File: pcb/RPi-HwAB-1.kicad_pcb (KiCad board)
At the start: 6 copper layers, 65 x 56 mm, 131 parts, among them J1 GPIO, J2 Hirose_FH12-16S, J3 TC2030, U1 CAT24C256, U10 MT41K256M16TW-107:P TR, U11 INA230AIRGTR, U12 MCP9804T-E/MC, U13 INA230AIRGTR, U14 INA230AIRGTR, U2 TPSM82903, U3 TLV74312PDBVR, U4 TPSM82903, U5 AP3441SHE-7B, U6 AP3441SHE-7B, U7 XC7A100T-FGG484, U9 MX25L12835F, Y1 SiT9365AI-2B2-33E200.000000

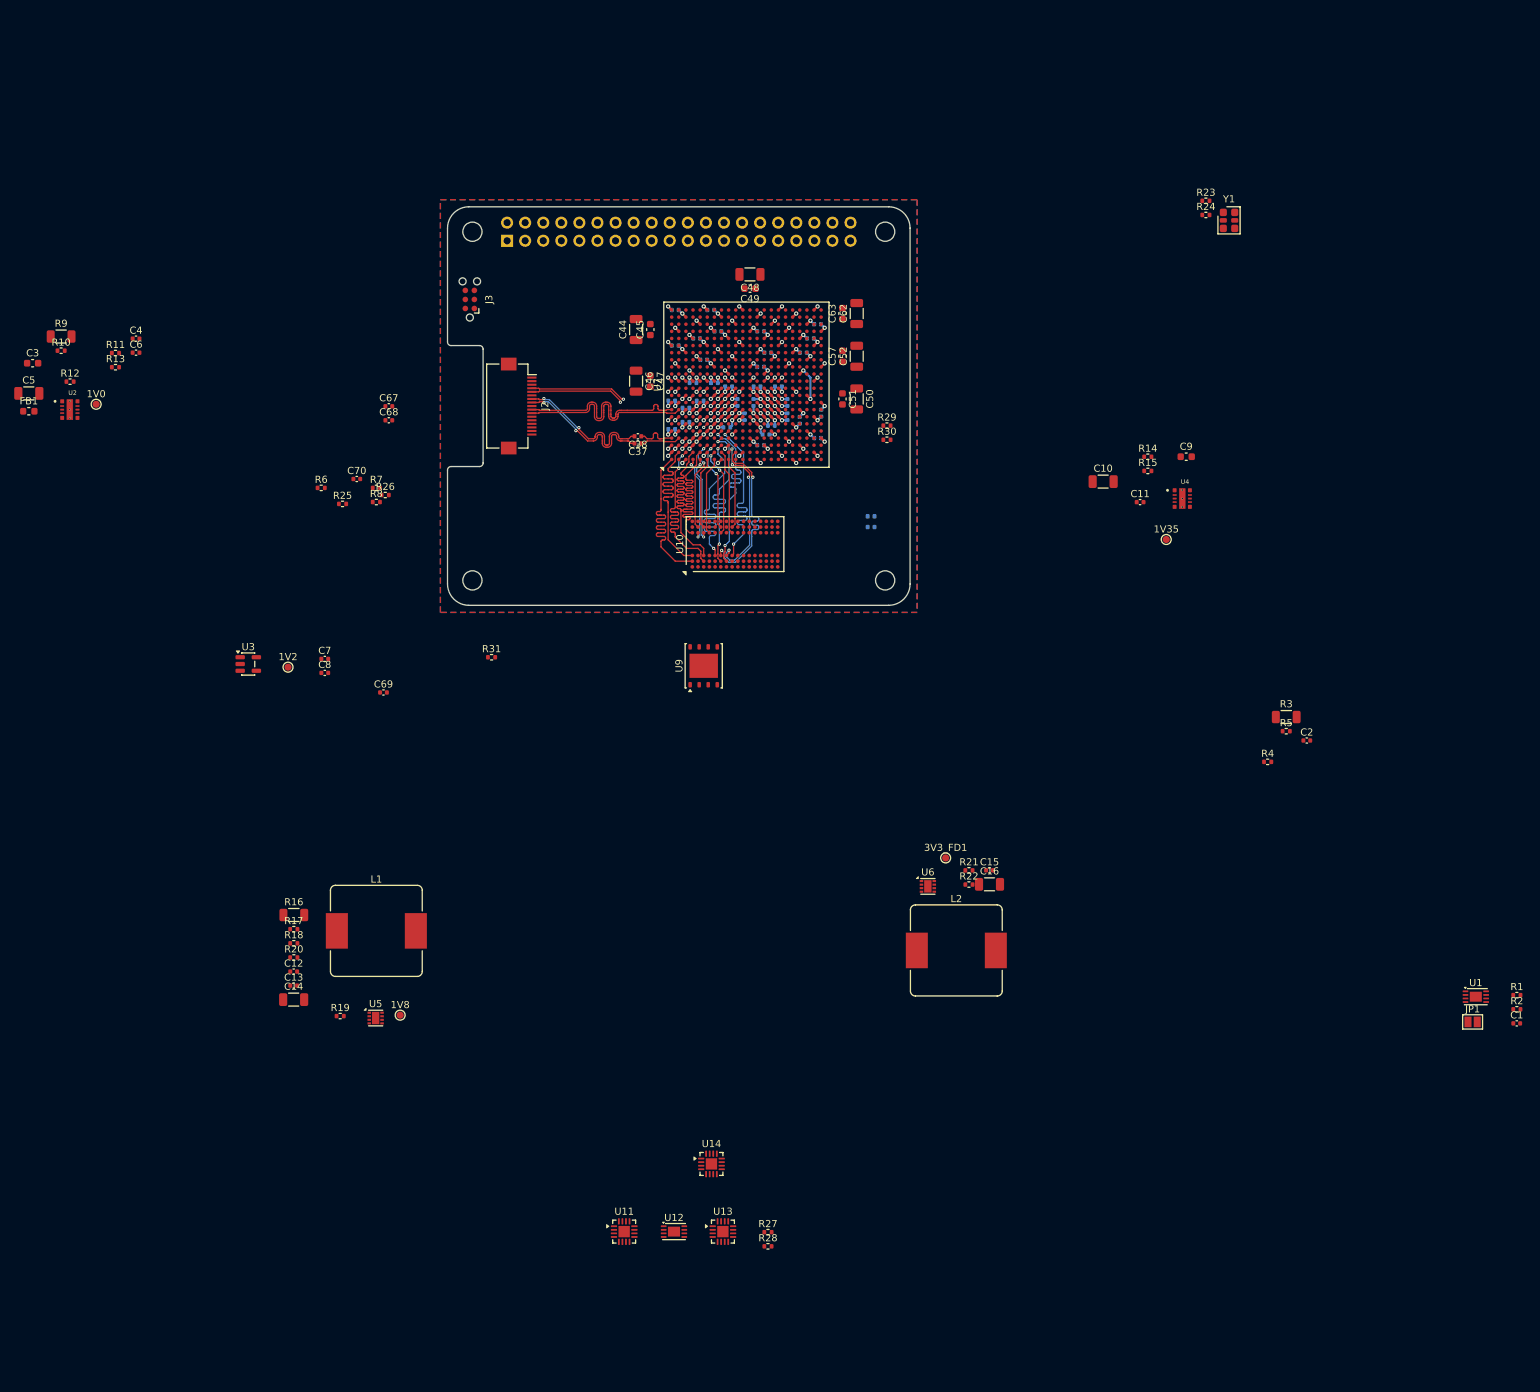
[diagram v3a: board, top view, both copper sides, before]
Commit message: restructured power, power plane layout
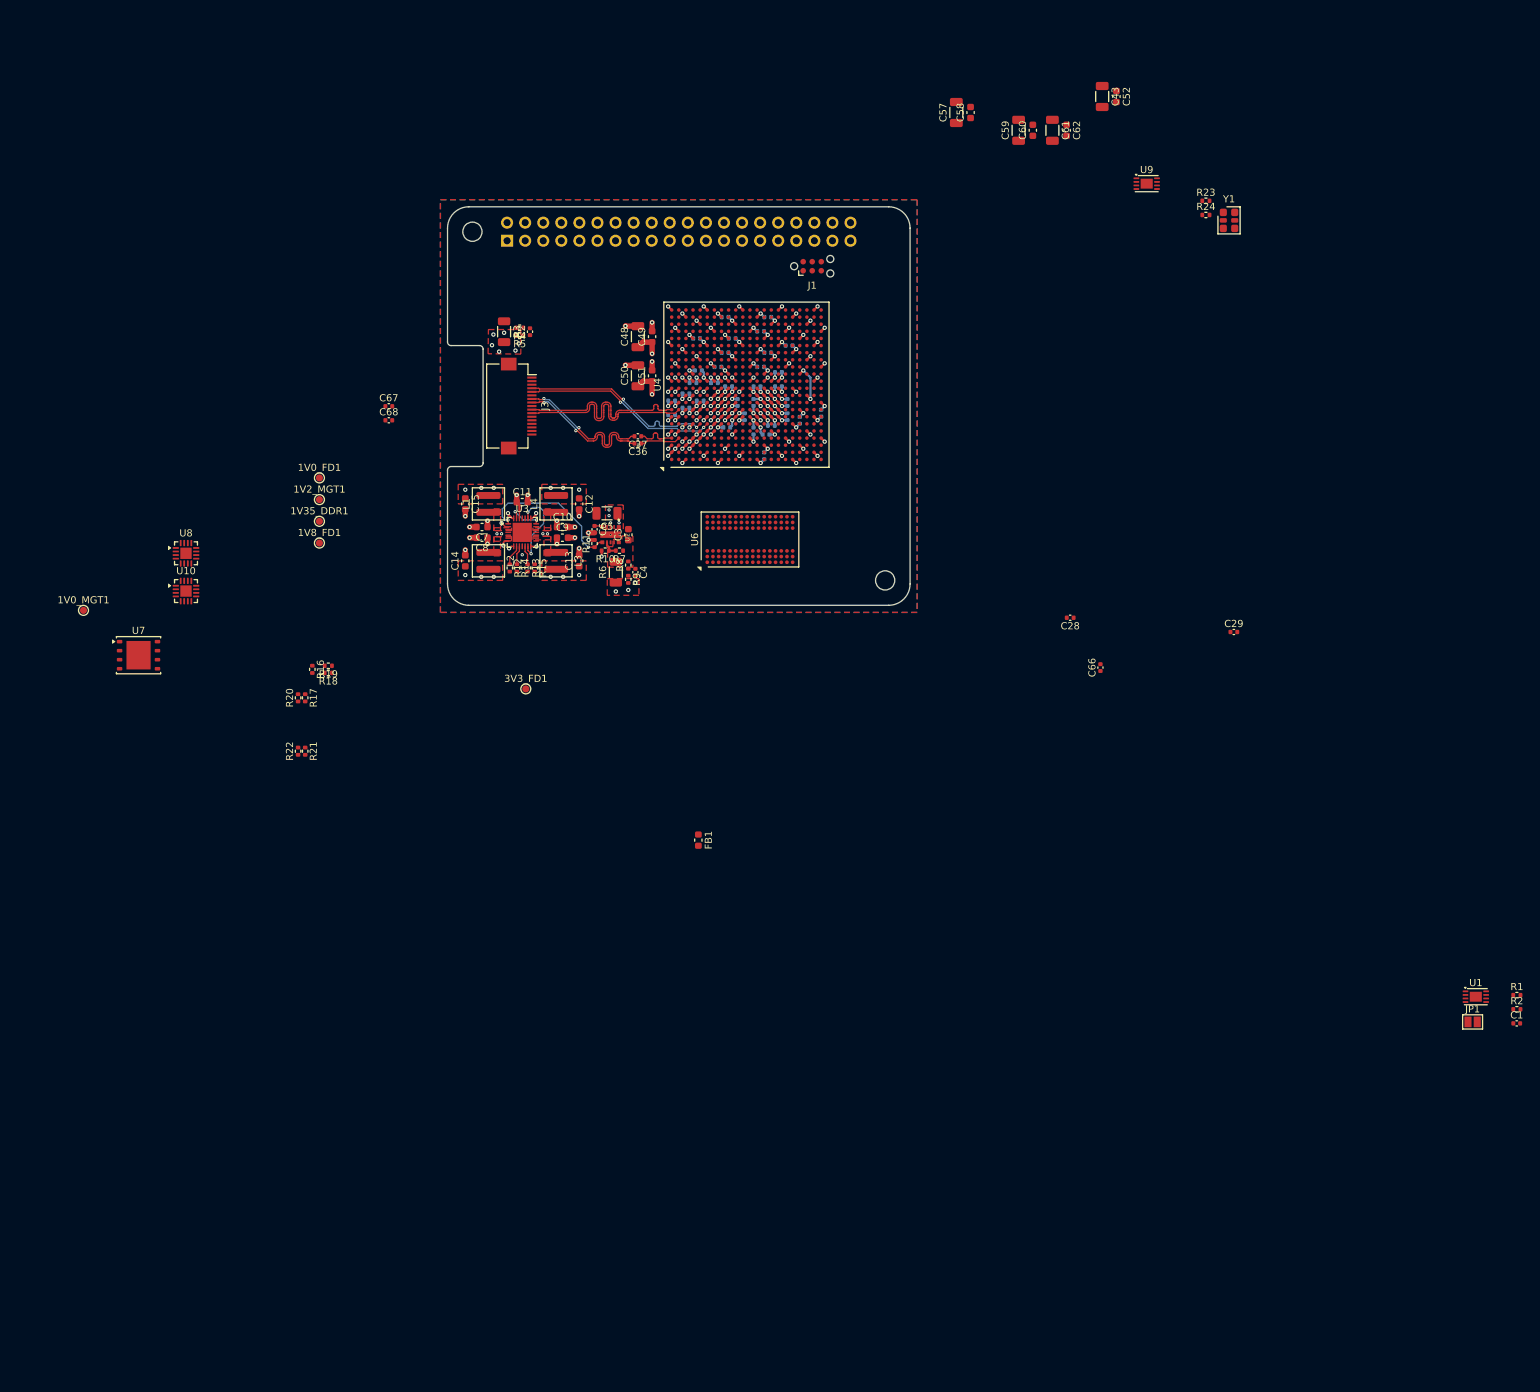
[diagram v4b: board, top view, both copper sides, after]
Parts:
- removed 1V0, 1V2, 1V35, 1V8: TestPoint, TestPoint:TestPoint_Pad_D1.0mm
- removed C69, C70: 0.1uF, Capacitor_SMD:C_0402_1005Metric
- removed MH2, MH3: MountingHole_2.7mm_M2.5, MountingHole:MountingHole_2.7mm_M2.5
- removed R25: 1K, Resistor_SMD:R_0402_1005Metric
- removed R26: 240 1%, Resistor_SMD:R_0402_1005Metric
- removed R27, R28: 4.7K, Resistor_SMD:R_0402_1005Metric
- removed R29: 2.2K, Resistor_SMD:R_0402_1005Metric
- removed R30: 100K, Resistor_SMD:R_0402_1005Metric
- removed R31: 100 1%, Resistor_SMD:R_0402_1005Metric
- removed U11, U13, U14: INA230AIRGTR, Package_DFN_QFN:VQFN-16-1EP_3x3mm_P0.5mm_EP1.6x1.6mm
- removed U12: MCP9804T-E/MC, Package_DFN_QFN:DFN-8-1EP_3x2mm_P0.5mm_EP1.7x1.4mm
- removed U5: AP3441SHE-7B, Package_DFN_QFN:DFN-8-1EP_2x2mm_P0.5mm_EP1.05x1.75mm
- added 1V0_FD1: TestPoint, TestPoint:TestPoint_Pad_D1.0mm, F.Cu at (82.0, 82.1)
- added 1V0_MGT1: TestPoint, TestPoint:TestPoint_Pad_D1.0mm, F.Cu at (48.8, 100.7)
- added 1V2_MGT1: TestPoint, TestPoint:TestPoint_Pad_D1.0mm, F.Cu at (82.0, 85.2)
- added 1V35_DDR1: TestPoint, TestPoint:TestPoint_Pad_D1.0mm, F.Cu at (82.0, 88.2)
- added 1V8_FD1: TestPoint, TestPoint:TestPoint_Pad_D1.0mm, F.Cu at (82.0, 91.2)
- added L3: 1.5uH, Inductor_SMD:L_Coilcraft_XAL4020-XXX, F.Cu at (115.2, 93.8)
- added L4: 1.5uH, Inductor_SMD:L_Coilcraft_XAL4020-XXX, F.Cu at (115.2, 85.8)
- added U8: INA230AIRGTR, Package_DFN_QFN:VQFN-16-1EP_3x3mm_P0.5mm_EP1.6x1.6mm, F.Cu at (63.2, 92.7)
- C10: value 10uF -> 2.2uF; footprint Capacitor_SMD:C_1206_3216Metric -> Capacitor_SMD:C_0603_1608Metric
- C11: value 4.7nF -> 2.2uF; footprint Capacitor_SMD:C_0402_1005Metric -> Capacitor_SMD:C_0603_1608Metric
- C12, C15: value 4.7nF -> 22uF; footprint Capacitor_SMD:C_0402_1005Metric -> Capacitor_SMD:C_0603_1608Metric
- C13: value 0.1uF -> 22uF; footprint Capacitor_SMD:C_0402_1005Metric -> Capacitor_SMD:C_0603_1608Metric
- C14: value 10uF -> 22uF; footprint Capacitor_SMD:C_1206_3216Metric -> Capacitor_SMD:C_0603_1608Metric
- C16, C44, C46: value 10uF -> 0.1uF; footprint Capacitor_SMD:C_1206_3216Metric -> Capacitor_SMD:C_0402_1005Metric; moved to B.Cu
- C28, C29, C36, C66: moved to F.Cu
- C38: moved to B.Cu
- C43, C59, C61: value 0.1uF -> 10uF; footprint Capacitor_SMD:C_0402_1005Metric -> Capacitor_SMD:C_1206_3216Metric; moved to F.Cu
- C45, C47, C63: value 4.7uF -> 0.1uF; footprint Capacitor_SMD:C_0603_1608Metric -> Capacitor_SMD:C_0402_1005Metric; moved to B.Cu
- C52, C62: value 10uF -> 4.7uF; footprint Capacitor_SMD:C_1206_3216Metric -> Capacitor_SMD:C_0603_1608Metric
- C57: value 4.7uF -> 10uF; footprint Capacitor_SMD:C_0603_1608Metric -> Capacitor_SMD:C_1206_3216Metric
- C58, C60: value 0.1uF -> 4.7uF; footprint Capacitor_SMD:C_0402_1005Metric -> Capacitor_SMD:C_0603_1608Metric; moved to F.Cu
- C7, C8: value 1uF -> 2.2uF; footprint Capacitor_SMD:C_0402_1005Metric -> Capacitor_SMD:C_0603_1608Metric
- C9: value 22uF -> 2.2uF
- L1, L2: value 2.2uH -> 1.5uH; footprint Inductor_SMD:L_Bourns_SRP1245A -> Inductor_SMD:L_Coilcraft_XAL4020-XXX
- R10: value 10K 1% -> 15K 1%
- R11, R12: value 10 -> 20K
- R13, R14: value 15K 1% -> 20K
- R15: value 12K 1% -> 20K
- R16: value 0.005 -> 100 1%; footprint Resistor_SMD:R_1206_3216Metric -> Resistor_SMD:R_0402_1005Metric
- R17: value 30K 1% -> 4.7K
- R18: value 10 -> 4.7K
- R19: value 10 -> 1K
- R20: value 15K 1% -> 240 1%
- R21: value 113K 1% -> 4.7K
- R22: value 24.9K 1% -> 4.7K
- R23: value 4.7K -> 2.2K
- R24: value 4.7K -> 100K
- R6: value 100K -> 0.005; footprint Resistor_SMD:R_0402_1005Metric -> Resistor_SMD:R_1206_3216Metric
- R7: value 100K -> 10K 1%
- R8: value 100K -> 10
- R9: value 0.005 -> 10; footprint Resistor_SMD:R_1206_3216Metric -> Resistor_SMD:R_0402_1005Metric
- U10: value MT41K256M16TW-107:P TR -> INA230AIRGTR; footprint Package_BGA:Micron_FBGA-96_7.5x13.5mm_Layout9x16_P0.8mm -> Package_DFN_QFN:VQFN-16-1EP_3x3mm_P0.5mm_EP1.6x1.6mm
- U3: value TLV74312PDBVR -> MAX20029; footprint Package_TO_SOT_SMD:SOT-23-5 -> Package_DFN_QFN:WQFN-28-1EP_4x4mm_P0.4mm_EP2.7x2.7mm
- U4: value TPSM82903 -> XC7A100T-FGG484; footprint library:TPSM82903SISR -> library:Xilinx_FGG484
- U6: value AP3441SHE-7B -> MT41K256M16TW-107:P TR; footprint Package_DFN_QFN:DFN-8-1EP_2x2mm_P0.5mm_EP1.05x1.75mm -> Package_BGA:Micron_FBGA-96_7.5x13.5mm_Layout9x16_P0.8mm
- U7: value XC7A100T-FGG484 -> MX25L12835F; footprint library:Xilinx_FGG484 -> Package_SON:WSON-8-1EP_6x5mm_P1.27mm_EP3.4x4mm
- U9: value MX25L12835F -> MCP9804T-E/MC; footprint Package_SON:WSON-8-1EP_6x5mm_P1.27mm_EP3.4x4mm -> Package_DFN_QFN:DFN-8-1EP_3x2mm_P0.5mm_EP1.7x1.4mm
- moved C2 123.4 mm to (111.6, 61.5), turned to 90 degrees
- moved R3 122.5 mm to (108.0, 61.5), turned to -90 degrees
- moved R4 121.5 mm to (110.1, 61.0), turned to 180 degrees
- moved R5 121.2 mm to (110.1, 62.1), turned to 180 degrees
- moved FB1 111.7 mm to (135.2, 133.0), turned to -90 degrees
- moved R22 96.1 mm to (79.0, 120.5), turned to 90 degrees
- moved R21 94.8 mm to (80.0, 120.5), turned to -90 degrees
- moved U7 93.5 mm to (56.6, 107.0), turned to 0 degrees
- moved U9 92.0 mm to (198.2, 40.8), turned to 0 degrees
- moved R14 90.0 mm to (109.8, 94.8), turned to -90 degrees
- moved C15 89.9 mm to (102.5, 85.8), turned to -90 degrees
- moved C9 88.4 mm to (116.2, 90.5)
- moved R15 87.2 mm to (112.2, 94.8), turned to -90 degrees
- moved C3 87.1 mm to (125.4, 90.1), turned to 90 degrees
- moved C11 86.8 mm to (110.5, 85.5)
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- renumbered J3 to J1, J1 to J2, J2 to J3
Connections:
- C11 pad 1: Net-(U4-SS/TR) -> /Main Power/5V0_N
- C12 pad 1: /Main Power/1V8/1V8_P -> /Main Power/1V2_MGT
- C12 pad 2: /Main Power/1V8/1V8_FB -> GND
- C13 pad 1: /Main Power/1V8_SENS_N -> /Main Power/3V3_FD
- C13 pad 2: /Main Power/1V8_SENS_P -> GND
- C14 pad 1: /Main Power/5V0_N -> /Main Power/1V35_DDR
- C15 pad 1: /Main Power/3V3_FD -> /Main Power/1V8_FD
- C15 pad 2: /Main Power/3V3/3V3_FB -> GND
- C16 pad 1: /Main Power/5V0_N -> GND
- C16 pad 2: GND -> /Main Power/3V3_FD
- C28 pad 1: GND -> /FPGA/FPGA 34, 35/DDR_SYSCLK_N
- C28 pad 2: /Main Power/3V3_FD -> Net-(Y1-OUT-)
- C29 pad 1: /FPGA/FPGA 3/DDR_SYSCLK_N -> /FPGA/FPGA 34, 35/DDR_SYSCLK_P
- C29 pad 2: Net-(Y1-OUT-) -> Net-(Y1-OUT+)
- C30 pad 1: /FPGA/FPGA 3/DDR_SYSCLK_P -> GND
- C30 pad 2: Net-(Y1-OUT+) -> /Main Power/1V35_DDR
- C36 pad 1: GND -> /FPGA/FPGA 216/F2P_P
- C36 pad 2: /Main Power/1V35_DDR -> /Connectors/PCIE.F2P_N
- C37 pad 1: /FPGA/FPGA 4/F2P_P -> /FPGA/FPGA 216/F2P_N
- C37 pad 2: /Connectors/PCIE.F2P_N -> /Connectors/PCIE.F2P_P
- C38 pad 1: /FPGA/FPGA 4/F2P_N -> GND
- C38 pad 2: /Connectors/PCIE.F2P_P -> /Main Power/1V0_MGT
- C40 pad 2: /Main Power/1V0_MGT -> /Main Power/1V2_MGT
- C43 pad 1: GND -> /Main Power/1V0_FD
- C43 pad 2: /Main Power/1V2_MGT -> GND
- C44 pad 1: /Main Power/1V0_MGT -> GND
- C44 pad 2: GND -> /Main Power/1V0_FD
- C45 pad 1: /Main Power/1V0_MGT -> GND
- C45 pad 2: GND -> /Main Power/1V0_FD
- C46 pad 1: /Main Power/1V2_MGT -> GND
- C46 pad 2: GND -> /Main Power/1V0_FD
- C47 pad 1: /Main Power/1V2_MGT -> GND
- C47 pad 2: GND -> /Main Power/1V0_FD
- C48 pad 1: /Main Power/3V3_FD -> /Main Power/1V0_MGT
- C49 pad 1: /Main Power/3V3_FD -> /Main Power/1V0_MGT
- C50 pad 1: /Main Power/1V35_DDR -> /Main Power/1V2_MGT
- C51 pad 1: /Main Power/1V35_DDR -> /Main Power/1V2_MGT
- C57 pad 1: /Main Power/1V0_FD -> /Main Power/3V3_FD
- C58 pad 1: GND -> /Main Power/3V3_FD
- C58 pad 2: /Main Power/1V0_FD -> GND
- C59 pad 1: GND -> /Main Power/1V35_DDR
- C59 pad 2: /Main Power/1V0_FD -> GND
- C60 pad 1: GND -> /Main Power/1V35_DDR
- C60 pad 2: /Main Power/1V0_FD -> GND
- C61 pad 1: GND -> /Main Power/1V8_FD
- C61 pad 2: /Main Power/1V0_FD -> GND
- C63 pad 1: /Main Power/1V8_FD -> GND
- C63 pad 2: GND -> /Main Power/1V8_FD
- C66 pad 1: GND -> /Connectors/3V3_RPi
- C66 pad 2: /Main Power/1V8_FD -> GND
- C7 pad 1: /Main Power/1V8_FD -> /Main Power/5V0_N
- C8 pad 1: /Main Power/1V2_MGT -> /Main Power/5V0_N
- C9 pad 1: /Main Power/1V35_DDR -> /Main Power/5V0_N
- J2 pad 18: /Main Power/3V3/3V3_PG -> /Connectors/FPGA_PG
- L1 pad 1: /Main Power/1V8/1V8_LX -> /Main Power/Quad Buck/LX1
- L1 pad 2: /Main Power/1V8/1V8_P -> /Main Power/1V8_FD
- L2 pad 1: /Main Power/3V3/3V3_LX -> /Main Power/Quad Buck/LX2
- L2 pad 2: /Main Power/3V3_FD -> /Main Power/1V35_DDR
- R10 pad 1: /Main Power/1V0/1V0_P -> /Main Power/1V0/1V0_FB
- R10 pad 2: /Main Power/1V0/1V0_FB -> GND
- R11 pad 1: /Main Power/1V0_SENS_N -> /Main Power/1V0/1V0_PG
- R11 pad 2: /Main Power/1V0/1V0_P -> /Main Power/5V0_N
- R12 pad 1: /Main Power/1V0_SENS_P -> /Main Power/Quad Buck/1V2_PG
- R12 pad 2: /Main Power/1V0_FD -> /Main Power/5V0_N
- R13 pad 1: /Main Power/1V0/1V0_FB -> /Main Power/Quad Buck/3V3_PG
- R13 pad 2: GND -> /Main Power/5V0_N
- R14 pad 1: /Main Power/1V35_DDR -> /Main Power/Quad Buck/1V35_PG
- R14 pad 2: /Main Power/1V35/1V35_FB -> /Main Power/5V0_N
- R15 pad 1: /Main Power/1V35/1V35_FB -> /Main Power/Quad Buck/1V8_PG
- R15 pad 2: GND -> /Main Power/5V0_N
- R16 pad 1: /Main Power/1V8_FD -> /FPGA/FPGA 34, 35/DDR_SYSCLK_N
- R16 pad 2: /Main Power/1V8/1V8_P -> /FPGA/FPGA 34, 35/DDR_SYSCLK_P
- R17 pad 1: /Main Power/1V8/1V8_P -> /Main Power/1V35_DDR
- R17 pad 2: /Main Power/1V8/1V8_FB -> /FPGA/FPGA 34, 35/DDR_SYSCLK_P
- R18 pad 1: /Main Power/1V8_SENS_P -> /FPGA/FPGA 34, 35/DDR_SYSCLK_P
- R18 pad 2: /Main Power/1V8/1V8_P -> GND
- R19 pad 1: /Main Power/1V8_SENS_N -> Net-(U4G-MGTRREF_216)
- R19 pad 2: /Main Power/1V8_FD -> /Main Power/1V2_MGT
- R20 pad 1: /Main Power/1V8/1V8_FB -> Net-(U6-ZQ)
- R20 pad 2: GND -> /Main Power/1V35_DDR
- R21 pad 1: /Main Power/3V3_FD -> /Connectors/3V3_RPi
- R21 pad 2: /Main Power/3V3/3V3_FB -> /Connectors/I2C1.SDA
- R22 pad 1: /Main Power/3V3/3V3_FB -> /Connectors/3V3_RPi
- R22 pad 2: GND -> /Connectors/I2C1.SCL
- R23 pad 1: /Main Power/1V35_DDR -> /Main Power/3V3_FD
- R23 pad 2: /FPGA/FPGA 3/DDR_SYSCLK_P -> /Connectors/PCIE.DET_WAKE
- R24 pad 1: /FPGA/FPGA 3/DDR_SYSCLK_P -> GND
- R24 pad 2: GND -> /Connectors/PCIE.PWR_EN
- R6 pad 1: /Main Power/5V0_N -> /Main Power/1V0_FD
- R6 pad 2: /Main Power/1V0/1V0_PG -> /Main Power/1V0/1V0_P
- R7 pad 1: /Main Power/5V0_N -> /Main Power/1V0/1V0_P
- R7 pad 2: /Main Power/1V8/1V8_PG -> /Main Power/1V0/1V0_FB
- R8 pad 1: /Main Power/5V0_N -> /Main Power/1V0_SENS_N
- R8 pad 2: /Main Power/3V3/3V3_PG -> /Main Power/1V0/1V0_P
- R9 pad 1: /Main Power/1V0_FD -> /Main Power/1V0_SENS_P
- R9 pad 2: /Main Power/1V0/1V0_P -> /Main Power/1V0_FD
- U3 pad 1: /Main Power/1V8_FD -> /Main Power/1V0/1V0_PG
- U3 pad 2: GND -> /Main Power/5V0_N
- U3 pad 3: /Main Power/1V8_FD -> /Main Power/Quad Buck/LX1
- U3 pad 4: unconnected-(U3-NC-Pad4) -> GND
- U3 pad 5: /Main Power/1V2_MGT -> GND
- U9 pad 1: /Connectors/QSPI0.CS0n -> /Connectors/I2C1.SDA
- U9 pad 2: /Connectors/QSPI0.SIO1 -> /Connectors/I2C1.SCL
- U9 pad 3: /Connectors/QSPI0.SIO2 -> unconnected-(U9-Alert-Pad3)
- U9 pad 5: /Connectors/QSPI0.SIO0 -> GND
- U9 pad 6: /Connectors/QSPI0.SCLK -> GND
- U9 pad 7: /Connectors/QSPI0.SIO3 -> GND
- U9 pad 8: /Main Power/3V3_FD -> /Connectors/3V3_RPi
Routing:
- net /FPGA/FPGA 3/DQ13: track 26.7 -> 0.00 mm
- net /FPGA/FPGA 3/DQ15: track 26.7 -> 0.00 mm
- net /FPGA/FPGA 3/DQ9: track 26.7 -> 0.00 mm
- net /FPGA/FPGA 3/DQ12: track 26.7 -> 0.00 mm
- net /FPGA/FPGA 3/DDR_LDQS_P: track 25.3 -> 0.00 mm, vias 2 -> 0
- net /FPGA/FPGA 3/DQ2: track 25.3 -> 0.00 mm, vias 2 -> 0
- net /FPGA/FPGA 3/DQ6: track 25.3 -> 0.00 mm, vias 2 -> 0
- net /FPGA/FPGA 3/DQ4: track 25.3 -> 0.00 mm, vias 2 -> 0
- net /FPGA/FPGA 3/DQ11: track 25.2 -> 0.00 mm, vias 2 -> 0
- net /FPGA/FPGA 3/DQ0: track 25.2 -> 0.00 mm, vias 2 -> 0
- net /FPGA/FPGA 3/DDR_LDQS_N: track 22.5 -> 0.00 mm, vias 4 -> 0
- net /Main Power/1V0/1V0_PG: track 0.00 -> 21.1 mm, vias 0 -> 2
- net GND: track 106.1 -> 122.0 mm, vias 90 -> 110
- net /Main Power/Quad Buck/1V2_PG: track 0.00 -> 14.4 mm, vias 0 -> 2
- net /FPGA/FPGA 3/DQ14: track 13.0 -> 0.00 mm, vias 2 -> 0
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- added copper zone on F.Cu, net /Main Power/1V0/1V0_P
- added copper zone on F.Cu, net /Main Power/1V0_FD
- added copper zone on F.Cu, net /Main Power/1V2_MGT
- added copper zone on F.Cu, net /Main Power/1V35_DDR
- added copper zone on F.Cu, net /Main Power/1V8_FD
- added copper zone on F.Cu, net /Main Power/3V3_FD
- added copper zone on F.Cu, net /Main Power/5V0_N
- added copper zone on In2.Cu, net /Main Power/5V0_N
- added copper zone on F.Cu, net /Main Power/Quad Buck/LX1
- added copper zone on F.Cu, net /Main Power/Quad Buck/LX2
- added copper zone on F.Cu, net /Main Power/Quad Buck/LX3
- added copper zone on F.Cu, net /Main Power/Quad Buck/LX4

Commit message: updated sch plot
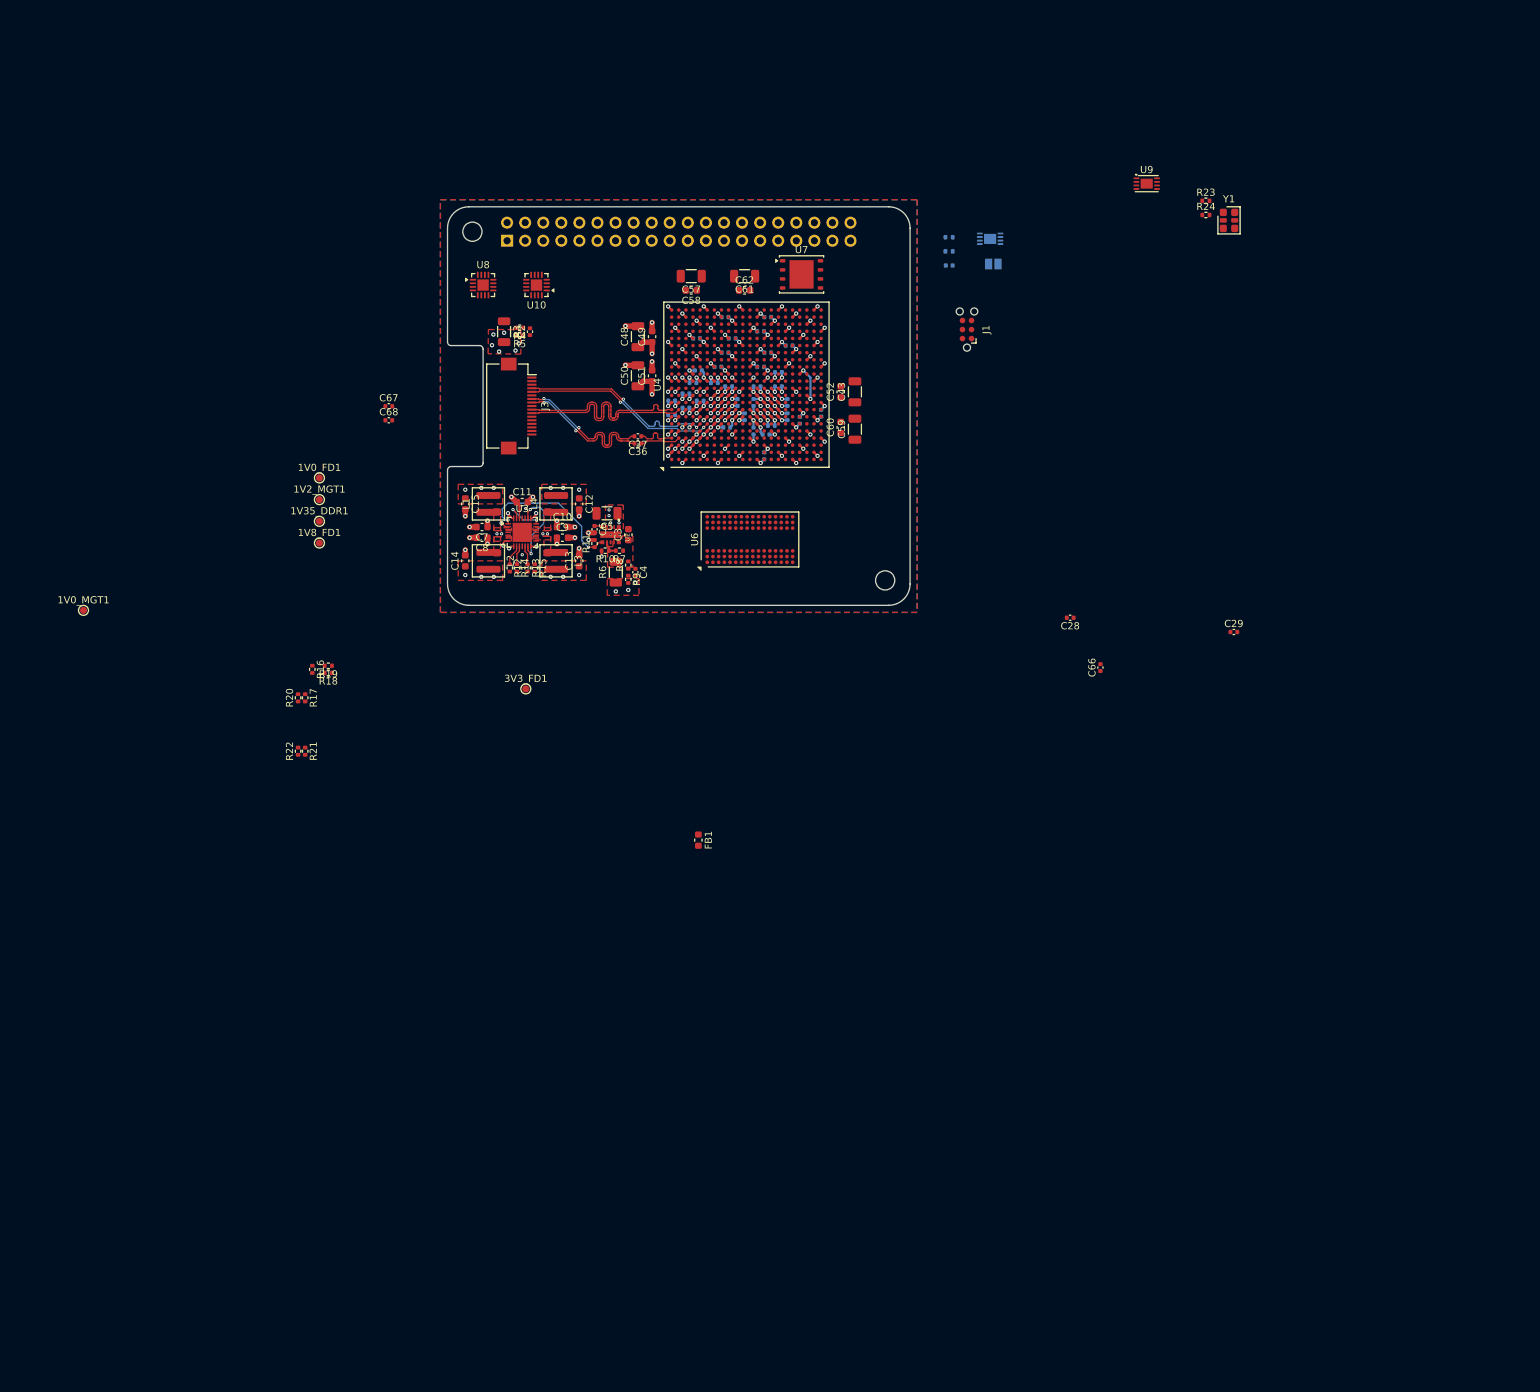
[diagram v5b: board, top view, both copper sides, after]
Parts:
- C1, JP1, R1, R2, U1: moved to B.Cu
- moved R1 133.1 mm to (170.5, 48.3), turned to 180 degrees
- moved R2 133.1 mm to (170.5, 50.3), turned to 180 degrees
- moved C1 133.1 mm to (170.5, 52.2), turned to 180 degrees
- moved U1 126.5 mm to (176.2, 48.5), turned to 180 degrees
- moved JP1 126.0 mm to (176.7, 52.0), turned to 180 degrees
- moved U7 107.4 mm to (149.8, 53.5)
- moved U10 65.4 mm to (112.5, 55.0), turned to 180 degrees
- moved C52 56.8 mm to (155.2, 70.0), turned to 90 degrees
- moved U8 56.2 mm to (105.0, 55.0)
- moved C43 54.1 mm to (157.2, 70.0), turned to 90 degrees
- moved C62 50.5 mm to (141.8, 55.8), turned to 0 degrees
- moved C60 49.7 mm to (155.2, 75.0)
- moved C59 47.9 mm to (157.2, 75.2)
- moved C61 47.9 mm to (141.8, 53.8), turned to 180 degrees
- moved C58 46.5 mm to (134.2, 55.8), turned to 180 degrees
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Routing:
- net /Main Power/Quad Buck/1V8_PG: track 5.06 -> 5.91 mm
- net GND: vias 110 -> 111
